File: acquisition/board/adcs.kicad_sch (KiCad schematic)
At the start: 16 parts

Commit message: Continued initial design
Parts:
- added R8: 100, symbol device:R
- added U6: ICE40UP5K_QFN48, symbol lattice-azonenberg:ICE40UP5K_QFN48
- gave numbers to parts that had none: 6
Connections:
- net CLIP_0: now also U6.6 (IOB_13b)
- net CLIP_1: now also U6.9 (IOB_16a)
- net CLIP_2: now also U6.10 (IOB_18a)
- net CLIP_3: now also U6.11 (IOB_20a)
- net CLIP_4: now also U6.12 (IOB_22a)
- net CLIP_5: now also U6.21 (IOB_23b)
- net CLIP_6: now also U6.13 (IOB_24a)
- net CLIP_7: now also U6.20 (IOB_25b_G3)
- net D7_4: now also U2.N12 (IO_L13N_T2_MRCC_14)
- net SYS_CLK_N: now also R8.2
- net SYS_CLK_P: now also R8.1
- net ADC_SDIO: now reaches U3.44 (SDIO/DCS)
- net ADC_SDIO: now also U1.44 (SDIO/DCS), U2.E13 (IO_L13N_T2_MRCC_15), U4.44 (SDIO/DCS), U5.44 (SDIO/DCS)
- net ADC_SCLK: now reaches U3.45 (SCLK/DFS)
- net ADC_SCLK: now also U1.45 (SCLK/DFS), U2.E11 (IO_L14P_T2_SRCC_15), U4.45 (SCLK/DFS), U5.45 (SCLK/DFS)
- net ADC1_CS_N: now reaches U3.46 (CSB)
- net ADC1_CS_N: now also U2.F4 (IO_L14P_T2_SRCC_35)
- net ADC1_OE_N: now reaches U3.47 (OEB)
- net ADC1_OE_N: now also U2.P15 (IO_L8P_T1_D11_14)
- net ADC1_PDWN: now reaches U3.48 (PDWN)
- net ADC2_CS_N: now reaches U4.46 (CSB)
- net ADC2_CS_N: now also U2.E5 (IO_L13N_T2_MRCC_35)
- net ADC2_OE_N: now reaches U4.47 (OEB)
- net ADC2_OE_N: now also U2.P16 (IO_L8N_T1_D12_14)
- net ADC2_PDWN: now reaches U4.48 (PDWN)
- net ADC0_CS_N: now reaches U1.46 (CSB)
- net ADC0_CS_N: now also U2.F3 (IO_L14N_T2_SRCC_35)
- net ADC0_OE_N: now reaches U1.47 (OEB)
- net ADC0_OE_N: now also U2.K12 (IO_0_14)
- net ADC0_PDWN: now reaches U1.48 (PDWN)
- net ADC3_CS_N: now reaches U2.C4 (IO_L12N_T1_MRCC_35)
- net ADC3_CS_N: now also U5.46 (CSB)
- net PLL_UWIRE_LE: now reaches U2.D3 (IO_L11N_T1_SRCC_35)
- net ICE40_SPI_SI: now reaches U2.K13 (IO_L5P_T0_D06_14)
- net ICE40_SPI_SI: now also U6.17 (IOB_33b_SPI_SI)
- net ICE40_SPI_SCK: now reaches U2.L13 (IO_L5N_T0_D07_14)
- net ICE40_SPI_SCK: now also U6.15 (IOB_34a_SPI_SCK)
- net ICE40_DONE: now reaches U2.L14 (IO_L4P_T0_D04_14)
- net ICE40_DONE: now also U6.7 (CDONE)
- net ICE40_SPI_CS_N: now reaches U2.M12 (IO_L6N_T0_D08_VREF_14)
- net ICE40_SPI_CS_N: now also U6.16 (IOB_35b_SPI_SS)
- net ICE40_SPI_SO: now reaches U2.M14 (IO_L4N_T0_D05_14)
- net ICE40_SPI_SO: now also U6.14 (IOB_32a_SPI_SO)
- net ICE40_RST_N: now reaches U2.M15 (IO_L3N_T0_DQS_EMCCLK_14)
- net ICE40_RST_N: now also U6.8 (CRESET_B)
- net ICE40_SPI_DQ3: now reaches U2.M16 (IO_L7P_T1_D09_14)
- net ICE40_SPI_DQ3: now also U6.19 (IOB_29b)
- net ICE40_SPI_DQ2: now reaches U2.N16 (IO_L7N_T1_D10_14)
- net ICE40_SPI_DQ2: now also U6.18 (IOB_31b)
- net ADC3_OE_N: now reaches U2.R15 (IO_L9P_T1_DQS_14)
- net ADC3_OE_N: now also U5.47 (OEB)
- net SYNC_OUT: now reaches U2.B16 (IO_L10N_T1_AD11N_15)
- net PLL_UWIRE_CLK: now reaches U2.C12 (IO_L11N_T1_SRCC_15)
- net PLL_UWIRE_DATA: now reaches U2.C13 (IO_L12N_T1_MRCC_15)
- net ADC3_PDWN: now reaches U5.48 (PDWN)
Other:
- note added: "Place termination close to FPGA balls"
- note added: "TODO: pullups/downs on ice40 config bus"
- note removed: "TODO: termination"
- company: (none) -> A. Zonenberg
- title: (none) -> Digitizer board

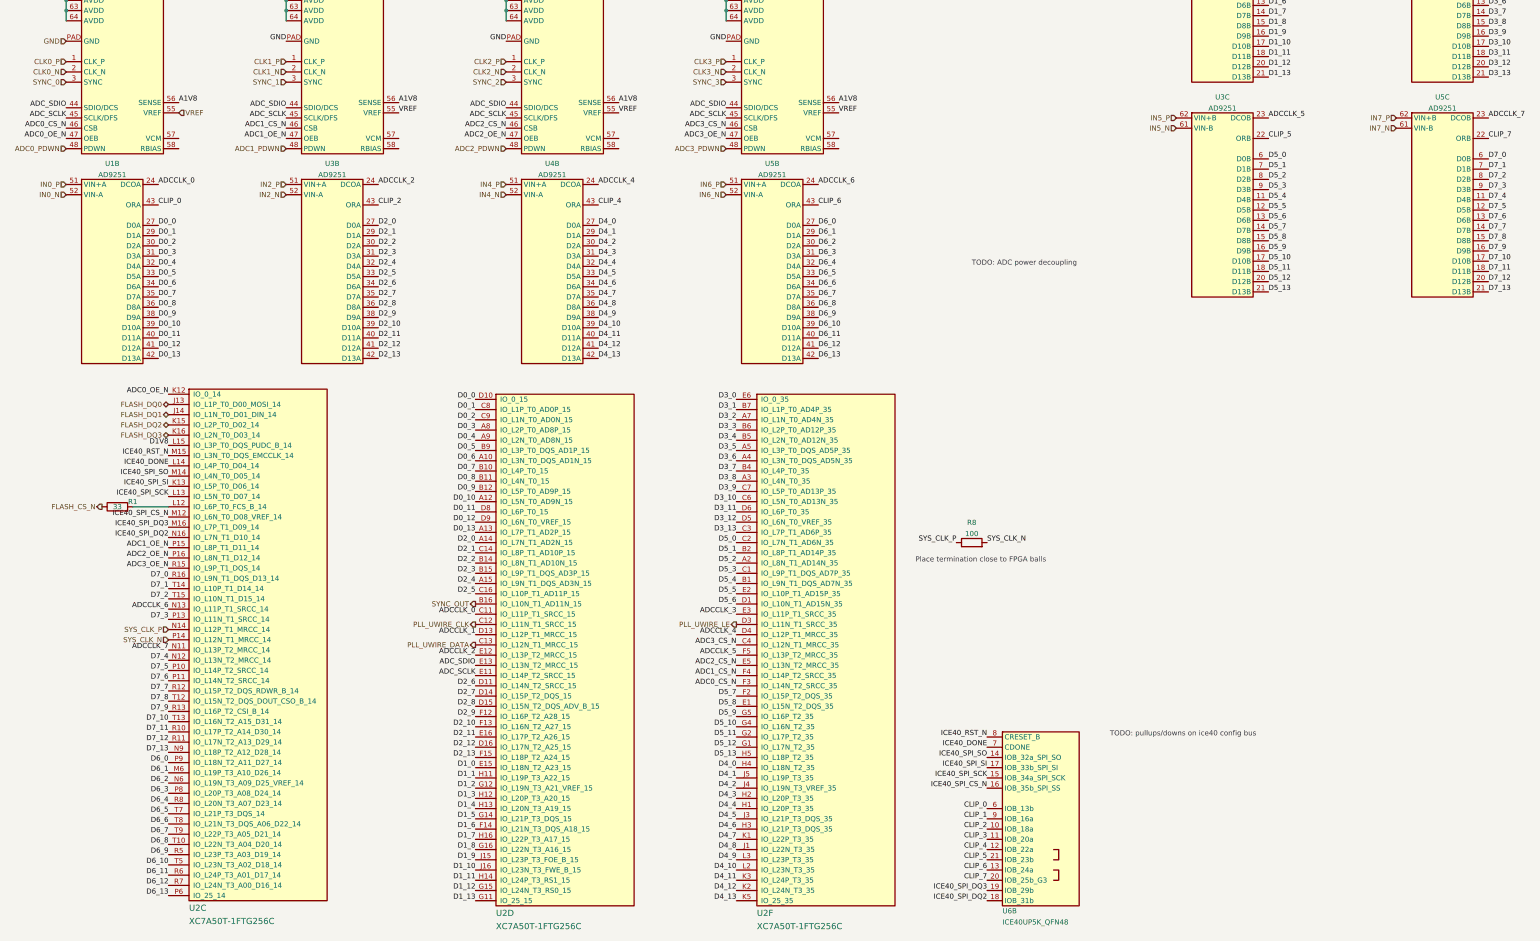
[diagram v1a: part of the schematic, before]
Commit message: Updated schematic with a lot of level shifting and support stuff, power decoupling, etc. Almost done except power supply and protection diodes
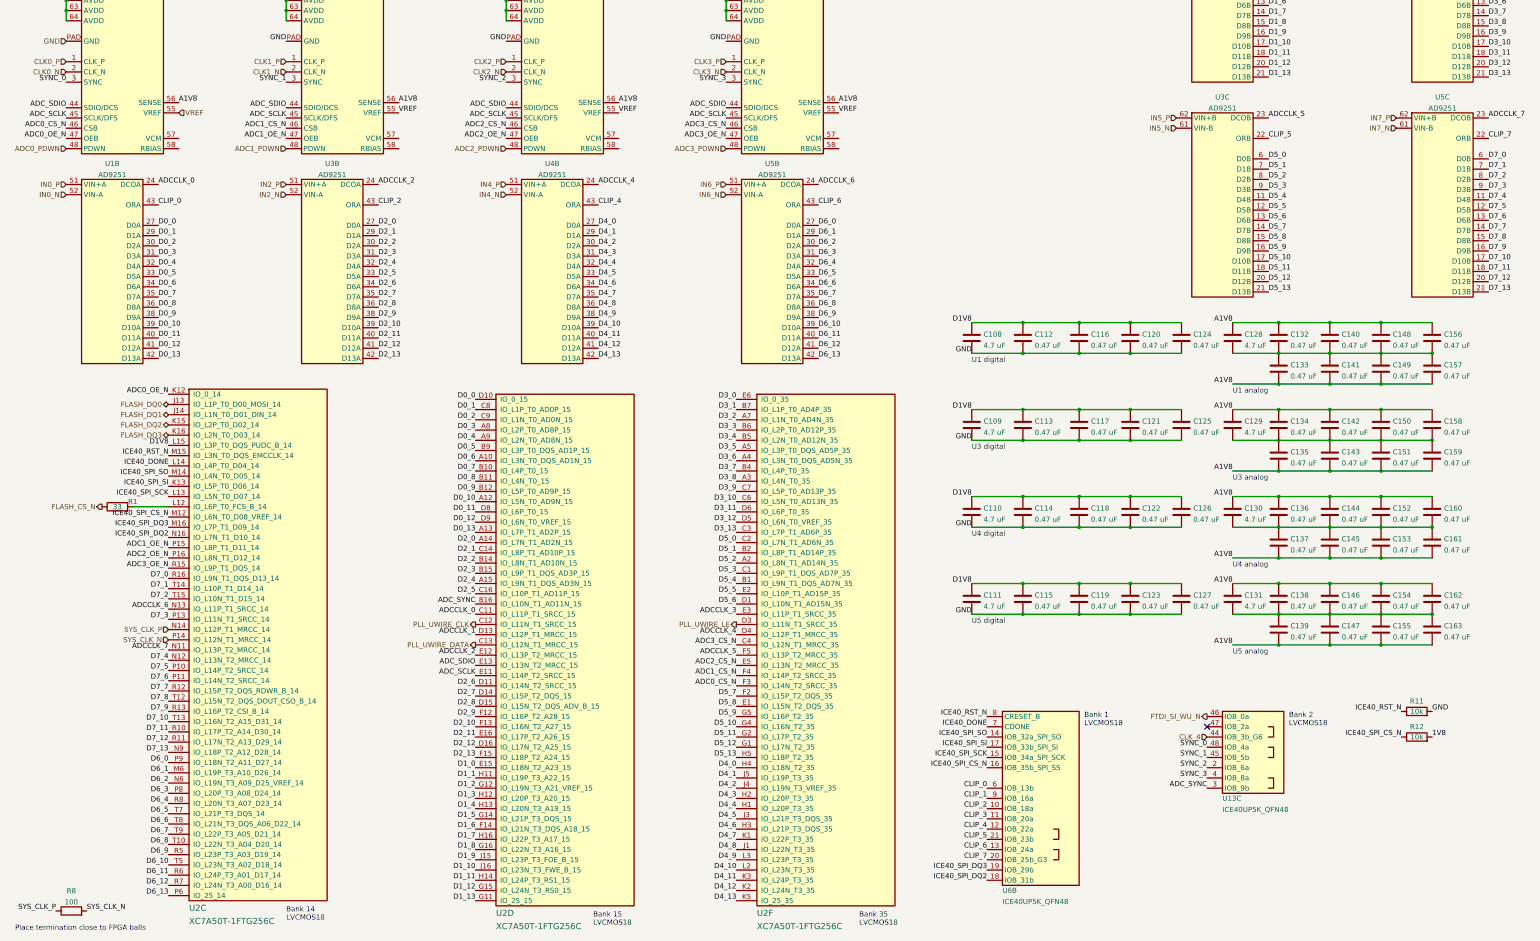
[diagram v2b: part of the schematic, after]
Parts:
- added C108, C109, C110, C111, C128, C129, C130, C131: 4.7 uF, symbol device:C
- added C112, C113, C114, C115, C116, C117, C118, C119, C120, C121, C122, C123, C124, C125, C126, C127, C132, C133, C134, C135, C136, C137, C138, C139, C140, C141, C142, C143, C144, C145, C146, C147, C148, C149, C150, C151, C152, C153, C154, C155, C156, C157, C158, C159, C160, C161, C162, C163: 0.47 uF, symbol device:C
- added R11, R12: 10k, symbol device:R
- added U13: ICE40UP5K_QFN48, symbol lattice-azonenberg:ICE40UP5K_QFN48
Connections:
- net A1V8: now also C128.1, C129.1, C130.1, C131.1, C132.1, C133.2, C134.1, C135.2, C136.1, C137.2, C138.1, C139.2, C140.1, C141.2, C142.1, C143.2, C144.1, C145.2, C146.1, C147.2, C148.1, C149.2, C150.1, C151.2, C152.1, C153.2, C154.1, C155.2, C156.1, C157.2, C158.1, C159.2, C160.1, C161.2, C162.1, C163.2
- net D1V8: now also C108.1, C109.1, C110.1, C111.1, C112.1, C113.1, C114.1, C115.1, C116.1, C117.1, C118.1, C119.1, C120.1, C121.1, C122.1, C123.1, C124.1, C125.1, C126.1, C127.1
- net GND: now also C108.2, C109.2, C110.2, C111.2, C112.2, C113.2, C114.2, C115.2, C116.2, C117.2, C118.2, C119.2, C120.2, C121.2, C122.2, C123.2, C124.2, C125.2, C126.2, C127.2, R11.2
- net ICE40_RST_N: now also R11.1
- net ICE40_SPI_CS_N: now also R12.1
- net SYNC_0: now also U13.48 (IOB_4a)
- net SYNC_1: now also U13.45 (IOB_5b)
- net SYNC_2: now also U13.2 (IOB_6a)
- net SYNC_3: now also U13.4 (IOB_8a)
- net SYNC_OUT renamed ADC_SYNC
- net ADC_SYNC: now also U13.3 (IOB_9b)
- new net: C128.2, C132.2, C133.1, C140.2, C141.1, C148.2, C149.1, C156.2, C157.1
- new net: C131.2, C138.2, C139.1, C146.2, C147.1, C154.2, C155.1, C162.2, C163.1
- new net: C129.2, C134.2, C135.1, C142.2, C143.1, C150.2, C151.1, C158.2, C159.1
- new net: C130.2, C136.2, C137.1, C144.2, C145.1, C152.2, C153.1, C160.2, C161.1
- new net 1V8: R12.2
- new net CLK_4: U13.44 (IOB_3b_G6)
- new net FTDI_SI_WU_N: U13.46 (IOB_0a)
- no-connect marks 0 -> 1
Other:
- note added: "Bank 1 LVCMOS18"
- note added: "Bank 14 LVCMOS18"
- note added: "Bank 15 LVCMOS18"
- note added: "Bank 2 LVCMOS18"
- note added: "Bank 35 LVCMOS18"
- note added: "U1 analog"
- note added: "U1 digital"
- note added: "U3 analog"
- note added: "U3 digital"
- note added: "U4 analog"
- note added: "U4 digital"
- note added: "U5 analog"
- note added: "U5 digital"
- note removed: "TODO: ADC power decoupling"
- note removed: "TODO: pullups/downs on ice40 config bus"
- moved on the sheet: R8, U6B

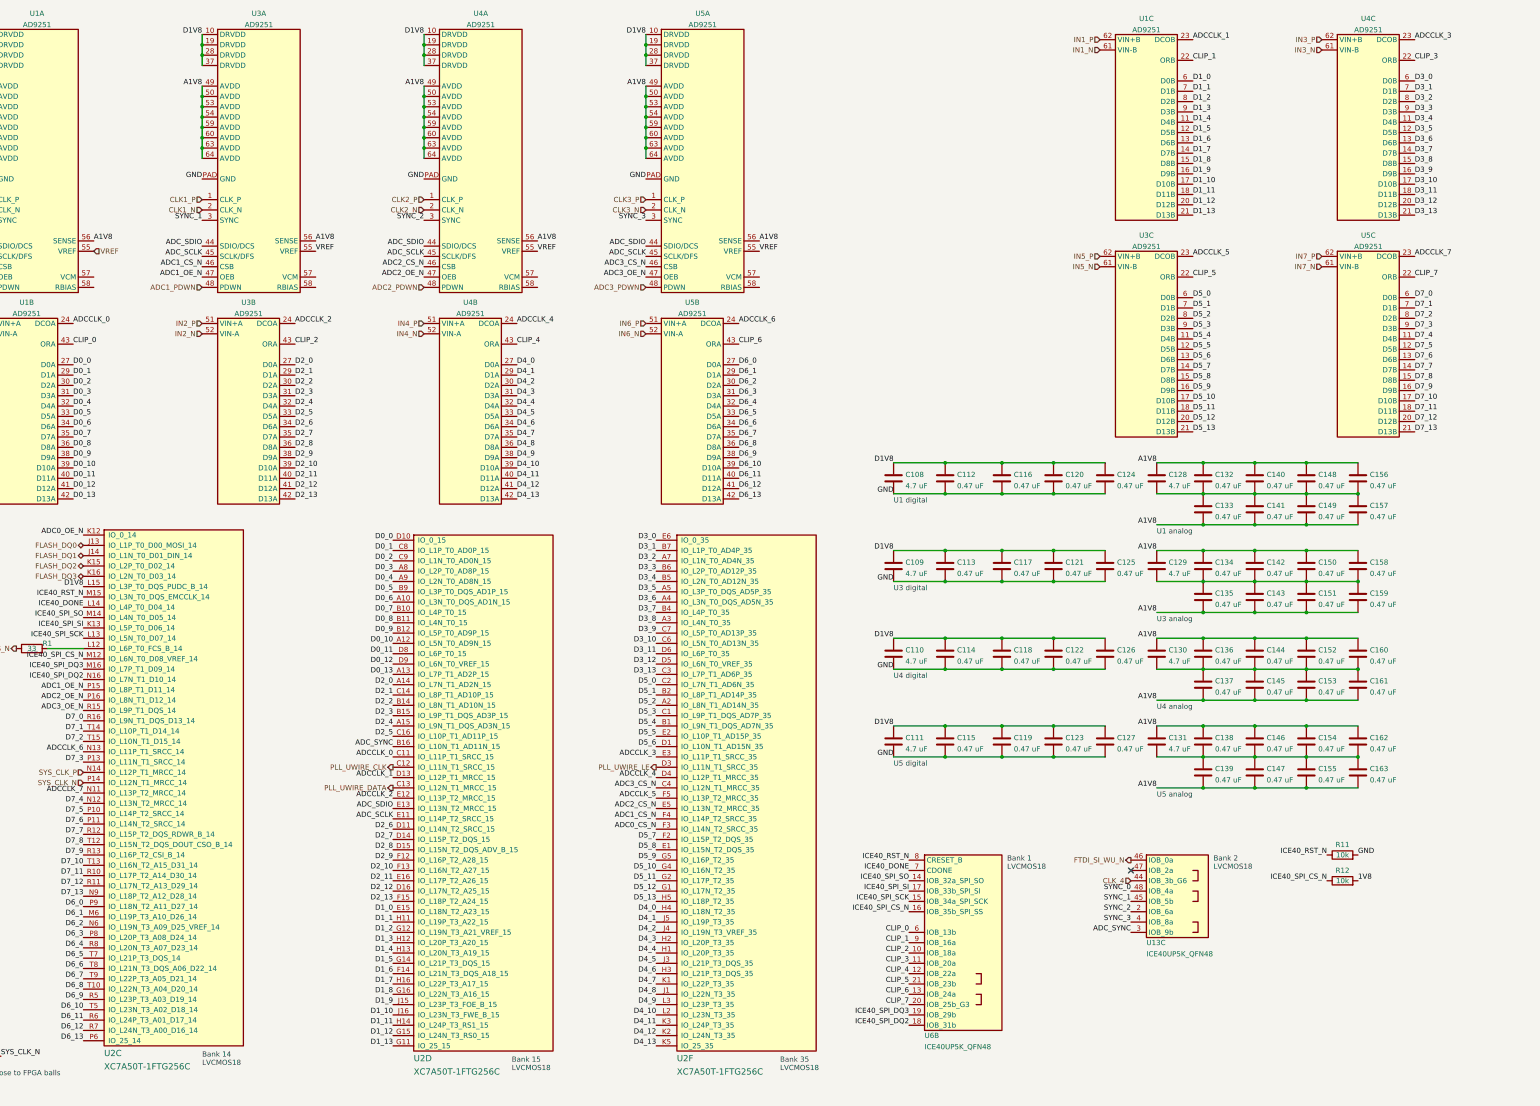
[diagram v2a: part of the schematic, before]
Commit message: Lots of progress on power supply design, added a bunch of test points, etc
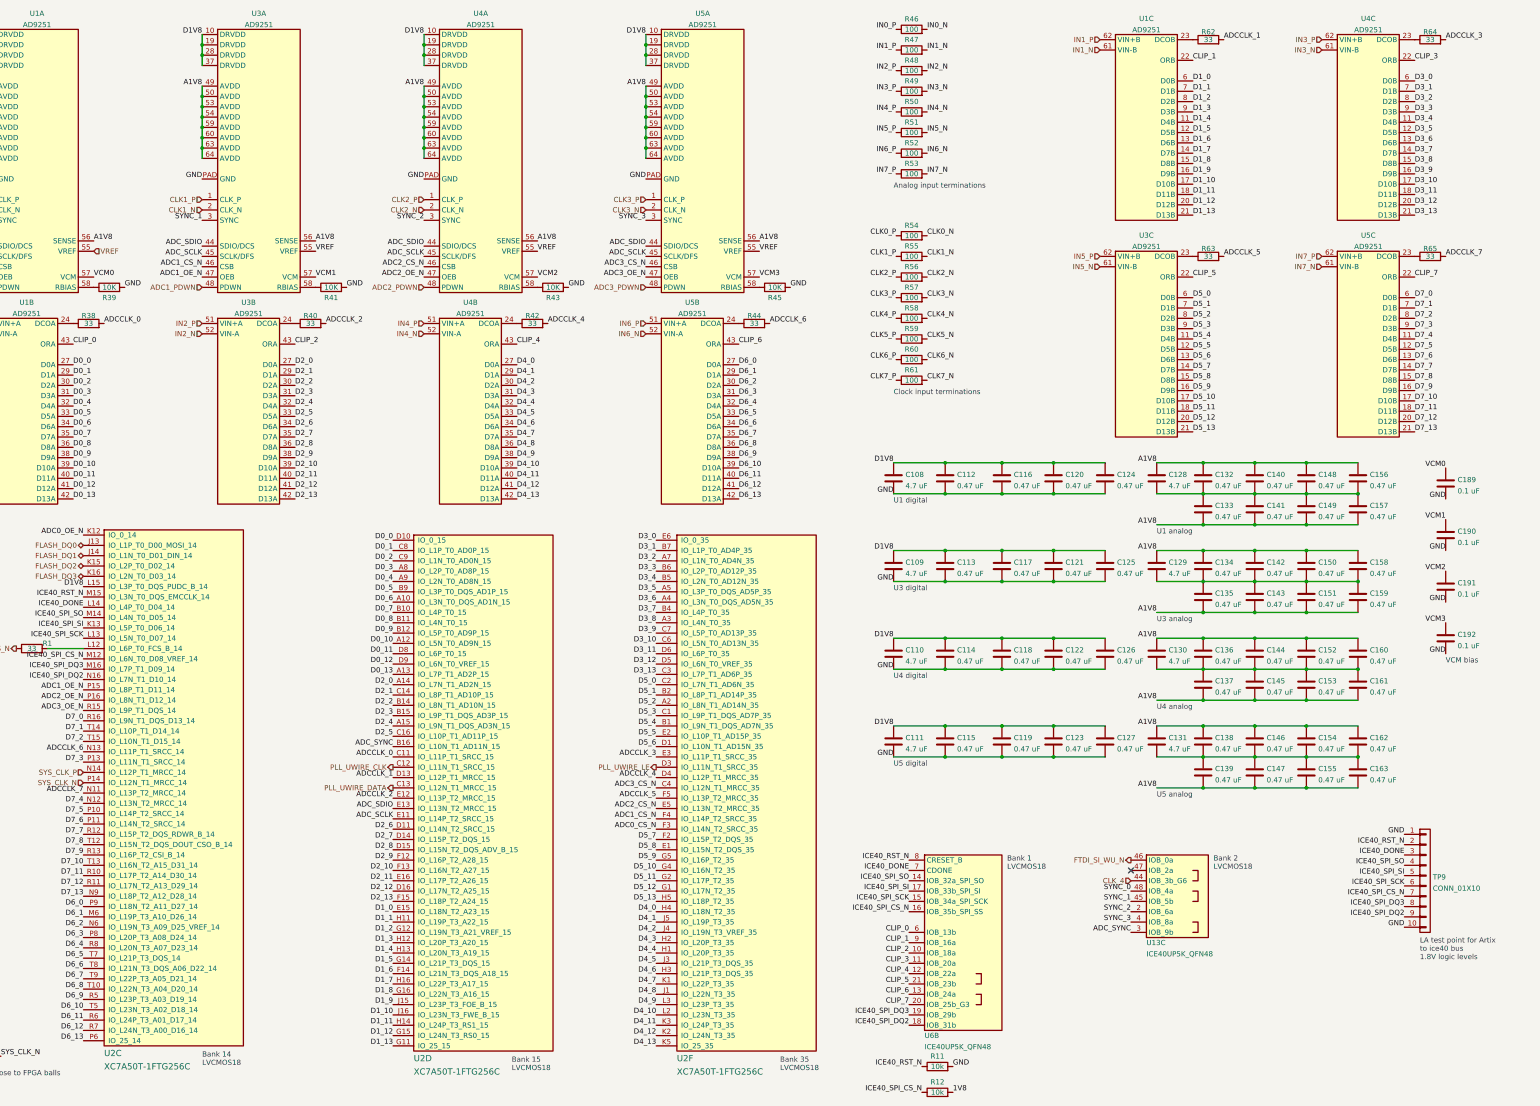
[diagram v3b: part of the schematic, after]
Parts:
- added C189, C190, C191, C192: 0.1 uF, symbol device:C
- added R38, R40, R42, R44, R62, R63, R64, R65: 33, symbol device:R
- added R39, R41, R43, R45: 10K, symbol device:R
- added R46, R47, R48, R49, R50, R51, R52, R53, R54, R55, R56, R57, R58, R59, R60, R61: 100, symbol device:R
- added TP9: CONN_01X10, symbol conn:CONN_01X10
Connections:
- net ADCCLK_0: now also R38.2; no longer U1.24 (DCOA)
- net ADCCLK_1: now also R62.2; no longer U1.23 (DCOB)
- net ADCCLK_2: now also R40.2; no longer U3.24 (DCOA)
- net ADCCLK_3: now also R64.2; no longer U4.23 (DCOB)
- net ADCCLK_4: now also R42.2; no longer U4.24 (DCOA)
- net ADCCLK_5: now also R63.2; no longer U3.23 (DCOB)
- net ADCCLK_6: now also R44.2; no longer U5.24 (DCOA)
- net ADCCLK_7: now also R65.2; no longer U5.23 (DCOB)
- net CLK0_N: now also R54.2
- net CLK0_P: now also R54.1
- net CLK1_N: now also R55.2
- net CLK1_P: now also R55.1
- net CLK2_N: now also R56.2
- net CLK2_P: now also R56.1
- net CLK3_N: now also R57.2
- net CLK3_P: now also R57.1
- net GND: now also C189.2, C190.2, C191.2, C192.2, R39.2, R41.2, R43.2, R45.2, TP9.1 (P1), TP9.10 (P10)
- net ICE40_DONE: now also TP9.3 (P3)
- net ICE40_RST_N: now also TP9.2 (P2)
- net ICE40_SPI_CS_N: now also TP9.7 (P7)
- net ICE40_SPI_DQ2: now also TP9.9 (P9)
- net ICE40_SPI_DQ3: now also TP9.8 (P8)
- net ICE40_SPI_SCK: now also TP9.6 (P6)
- net ICE40_SPI_SI: now also TP9.5 (P5)
- net ICE40_SPI_SO: now also TP9.4 (P4)
- net IN0_N: now also R46.2
- net IN0_P: now also R46.1
- net IN1_N: now also R47.2
- net IN1_P: now also R47.1
- net IN2_N: now also R48.2
- net IN2_P: now also R48.1
- net IN3_N: now also R49.2
- net IN3_P: now also R49.1
- net IN4_N: now also R50.2
- net IN4_P: now also R50.1
- net IN5_N: now also R51.2
- net IN5_P: now also R51.1
- net IN6_N: now also R52.2
- net IN6_P: now also R52.1
- net IN7_N: now also R53.2
- net IN7_P: now also R53.1
- net VCM1: now reaches U3.57 (VCM)
- net VCM1: now also C190.1
- net at U3.58 (RBIAS): now also R41.1
- net VCM2: now reaches U4.57 (VCM)
- net VCM2: now also C191.1
- net at U4.58 (RBIAS): now also R43.1
- net VCM0: now reaches U1.57 (VCM)
- net VCM0: now also C189.1
- net at U1.58 (RBIAS): now also R39.1
- net VCM3: now reaches U5.57 (VCM)
- net VCM3: now also C192.1
- net at U5.58 (RBIAS): now also R45.1
- new net: R63.1, U3.23 (DCOB)
- new net: R62.1, U1.23 (DCOB)
- new net: R40.1, U3.24 (DCOA)
- new net: R42.1, U4.24 (DCOA)
- new net: R64.1, U4.23 (DCOB)
- new net: R65.1, U5.23 (DCOB)
- new net: R44.1, U5.24 (DCOA)
- new net: R38.1, U1.24 (DCOA)
- new net CLK4_N: R58.2
- new net CLK4_P: R58.1
- new net CLK5_N: R59.2
- new net CLK5_P: R59.1
- new net CLK6_N: R60.2
- new net CLK6_P: R60.1
- new net CLK7_N: R61.2
- new net CLK7_P: R61.1
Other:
- note added: "Analog input terminations"
- note added: "Clock input terminations"
- note added: "LA test point for Artix to ice40 bus 1.8V logic levels"
- note added: "VCM bias"
- moved on the sheet: R11, R12

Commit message: More power supply work, added PLL loop filter, soft start, began assigning footprints
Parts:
- added C202, C203, C204, C205: 1 uF, symbol device:C
- added C206, C207, C208, C209: 0.1 uF, azonenberg_pcb:EIA_0402_CAP_NOSILK, symbol device:C
- C108, C109, C110, C111, C128, C129, C130, C131: footprint (none) -> azonenberg_pcb:EIA_0603_CAP_NOSILK
- C112, C113, C114, C115, C116, C117, C118, C119, C120, C121, C122, C123, C124, C125, C126, C127, C132, C133, C134, C135, C136, C137, C138, C139, C140, C141, C142, C143, C144, C145, C146, C147, C148, C149, C150, C151, C152, C153, C154, C155, C156, C157, C158, C159, C160, C161, C162, C163, C189, C190, C191, C192: footprint (none) -> azonenberg_pcb:EIA_0402_CAP_NOSILK
- R1, R11, R12, R38, R39, R40, R41, R42, R43, R44, R45, R46, R47, R48, R49, R50, R51, R52, R53, R54, R55, R56, R57, R58, R59, R60, R61, R62, R63, R64, R65, R8: footprint (none) -> azonenberg_pcb:EIA_0402_RES_NOSILK
- TP9: footprint (none) -> azonenberg_pcb:CONN_HEADER_2.54MM_1x10
- U2: footprint (none) -> azonenberg_pcb:BGA_256_17x17_FULLARRAY_1MM_0.4MM_FTG256
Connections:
- net GND: now also C202.2, C203.2, C204.2, C205.2, C206.2, C207.2, C208.2, C209.2
- net VREF: now also C202.1, C203.1, C204.1, C205.1, C206.1, C207.1, C208.1, C209.1
- net A1V8 renamed A1V8_1
- net A1V8_1: no longer C130.1, C131.1, C136.1, C137.2, C138.1, C139.2, C144.1, C145.2, C146.1, C147.2, C152.1, C153.2, C154.1, C155.2, C160.1, C161.2, C162.1, C163.2, U4.49 (AVDD), U4.50 (AVDD), U4.53 (AVDD), U4.54 (AVDD), U4.56 (SENSE), U4.59 (AVDD), U4.60 (AVDD), U4.63 (AVDD), U4.64 (AVDD), U5.49 (AVDD), U5.50 (AVDD), U5.53 (AVDD), U5.54 (AVDD), U5.56 (SENSE), U5.59 (AVDD), U5.60 (AVDD), U5.63 (AVDD), U5.64 (AVDD)
- new net A1V8_2: C130.1, C131.1, C136.1, C137.2, C138.1, C139.2, C144.1, C145.2, C146.1, C147.2, C152.1, C153.2, C154.1, C155.2, C160.1, C161.2, C162.1, C163.2, U4.49 (AVDD), U4.50 (AVDD), U4.53 (AVDD), U4.54 (AVDD), U4.56 (SENSE), U4.59 (AVDD), U4.60 (AVDD), U4.63 (AVDD), U4.64 (AVDD), U5.49 (AVDD), U5.50 (AVDD), U5.53 (AVDD), U5.54 (AVDD), U5.56 (SENSE), U5.59 (AVDD), U5.60 (AVDD), U5.63 (AVDD), U5.64 (AVDD)
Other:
- note added: "Reference input is 7.5K ohm per ADC 4 in parallel is 1.875K equivalent At 1V that's 533 uA load"
- moved on the sheet: R46, R47, R48, R49, R50, R51, R52, R53, R54, R55, R56, R57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
